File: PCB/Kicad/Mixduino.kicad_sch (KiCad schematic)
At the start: 4 parts

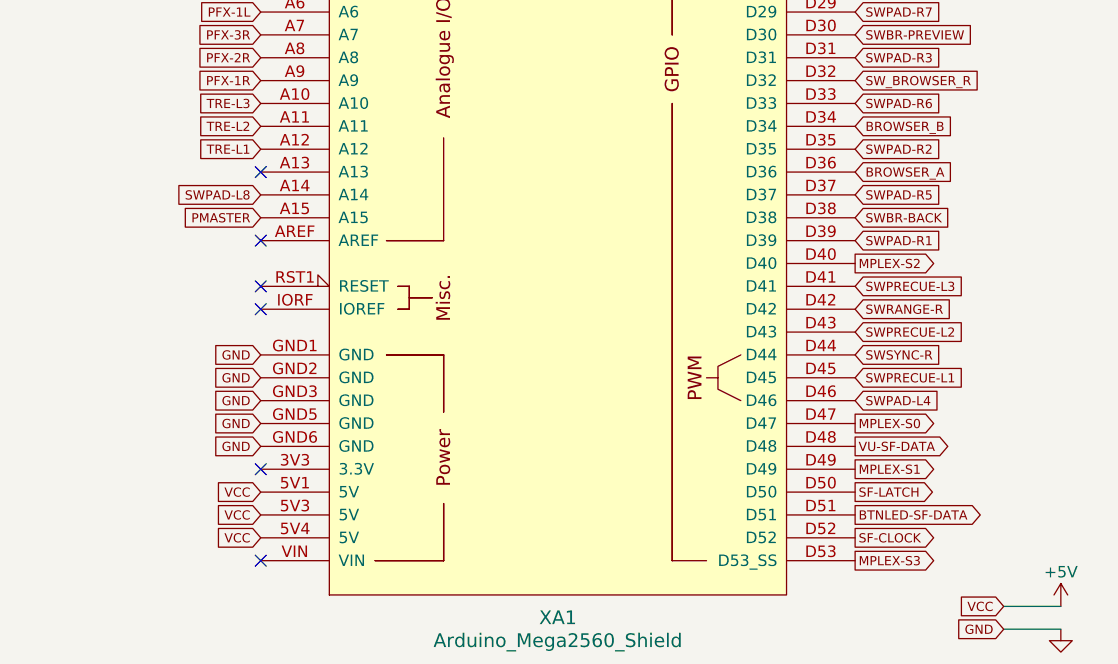
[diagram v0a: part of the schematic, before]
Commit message: mistake fixed
added another latch pin for feedback leds SReg.
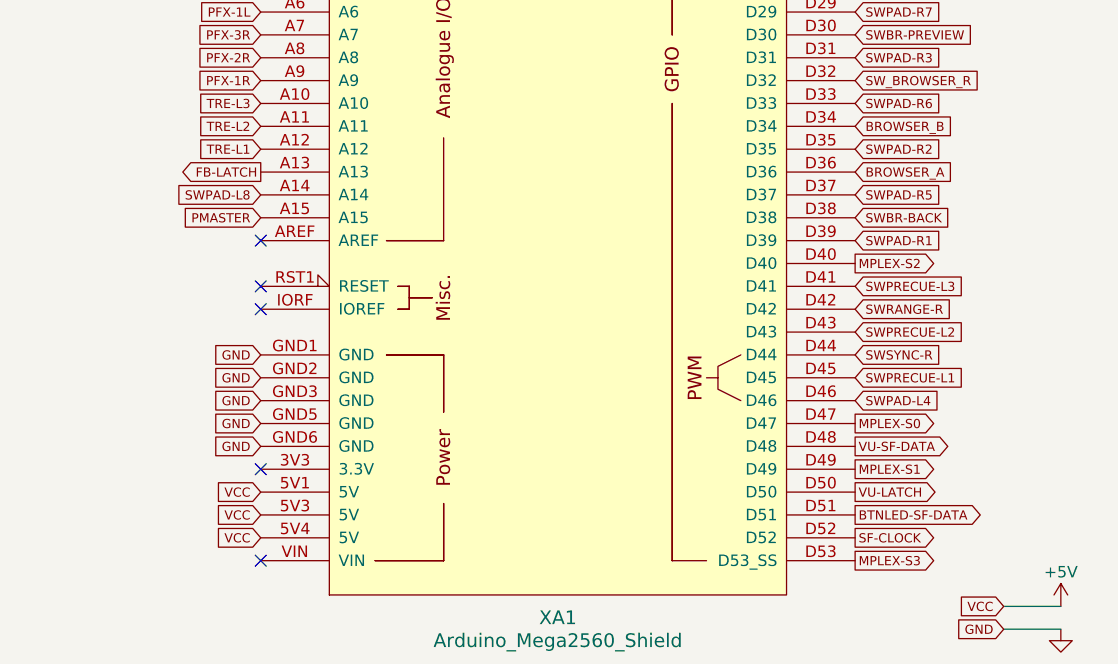
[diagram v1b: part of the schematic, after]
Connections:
- net FB-LATCH: now reaches XA1.A13
- net SF-LATCH renamed VU-LATCH
- no-connect marks 10 -> 9
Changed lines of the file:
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@@
   (no_connect (at 127.635 64.77))
   (no_connect (at 127.635 67.31))
-  (no_connect (at 127.635 105.41))
   (no_connect (at 127.635 113.03))
   (no_connect (at 127.635 118.11))
@@
     )
   )
+  (global_label "FB-LATCH" (shape output) (at 127.635 105.41 180)
+    (effects (font (size 1.016 1.016)) (justify right))
+    (property "Intersheet References" "${INTERSHEET_REFS}" (id 0) (at 119.9473 105.4735 0)
+      (effects (font (size 1.016 1.016)) (justify right) hide)
+    )
+  )
   (global_label "SWPAD-L8" (shape input) (at 127.635 107.95 180)
     (effects (font (size 1.016 1.016)) (justify right))
@@
     )
   )
-  (global_label "SF-LATCH" (shape output) (at 193.675 140.97 0)
+  (global_label "VU-LATCH" (shape output) (at 193.675 140.97 0)
     (effects (font (size 1.016 1.016)) (justify left))
     (property "Intersheet References" "${INTERSHEET_REFS}" (id 0) (at 203.2496 140.9065 0)

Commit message: schematic updated
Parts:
- removed IC-POTS-1: 74HC4067D,653, Library:SOIC-24W_7.5x15.4mm_P1.27mm, symbol mixduino-mk2:74HC4067D,653
- added IC-MPLEX-1: MP-POTS, Library:SOIC-24W_7.5x15.4mm_P1.27mm, symbol mixduino-mk2:74HC4067D,653
- added IC-MPLEX-2: MP-BTNS, Library:SOIC-24W_7.5x15.4mm_P1.27mm, symbol mixduino-mk2:74HC4067D,653
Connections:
- net +5V: now also IC-MPLEX-1.24 (VCC), IC-MPLEX-2.24 (VCC)
- net BAS-L1: now also IC-MPLEX-1.21 (Y10)
- net BAS-L2: now also IC-MPLEX-1.20 (Y11)
- net BAS-L3: now also IC-MPLEX-1.19 (Y12)
- net FADER-L1: now also IC-MPLEX-1.8 (Y1)
- net FADER-L2: now also IC-MPLEX-1.7 (Y2)
- net FADER-L3: now also IC-MPLEX-1.6 (Y3)
- net FB-LATCH: now also XA1.D5; no longer XA1.A13
- net FILTER-L1: now also IC-MPLEX-1.2 (Y7)
- net FILTER-L2: now also IC-MPLEX-1.23 (Y8)
- net FILTER-L3: now also IC-MPLEX-1.22 (Y9)
- net GAIN-L1: now also XA1.A10; no longer XA1.A3
- net GAIN-L2: now also XA1.A9; no longer XA1.A2
- net GAIN-L3: now also XA1.A8; no longer XA1.A1
- net GND: now also IC-MPLEX-1.12 (GND), IC-MPLEX-1.15 (~E), IC-MPLEX-2.12 (GND), IC-MPLEX-2.15 (~E)
- net MID-L1: now also IC-MPLEX-1.18 (Y13)
- net MID-L2: now also IC-MPLEX-1.17 (Y14)
- net MID-L3: now also IC-MPLEX-1.16 (Y15)
- net MPLEX-A0: now also IC-MPLEX-1.1 (Z)
- net MPLEX-S0: now also IC-MPLEX-1.10 (S0), IC-MPLEX-2.10 (S0)
- net MPLEX-S1: now also IC-MPLEX-1.11 (S1), IC-MPLEX-2.11 (S1)
- net MPLEX-S2: now also IC-MPLEX-1.14 (S2), IC-MPLEX-2.14 (S2)
- net MPLEX-S3: now also IC-MPLEX-1.13 (S3), IC-MPLEX-2.13 (S3)
- net PFX-1L: now also XA1.A4; no longer XA1.A6
- net PFX-1R: now also XA1.A7; no longer XA1.A9
- net PFX-2L: now also XA1.A3; no longer XA1.A5
- net PFX-2R: now also XA1.A6; no longer XA1.A8
- net PFX-3L: now also XA1.A2; no longer XA1.A4
- net PFX-3R: now also XA1.A5; no longer XA1.A7
- net PITCH-L: now also IC-MPLEX-1.9 (Y0)
- net PITCH-R: now also IC-MPLEX-1.3 (Y6)
- net PMASTER: now also XA1.A14; no longer XA1.A15
- net PMIX-HP: now also IC-MPLEX-1.5 (Y4)
- net PVOL-HP: now also IC-MPLEX-1.4 (Y5)
- net SWCUE-L: now also IC-MPLEX-2.19 (Y12); no longer XA1.D22
- net SWCUE-R: now also XA1.D28; no longer XA1.D15 (D15_RX3)
- net SWFX1-L: now also XA1.D8; no longer XA1.D7
- net SWFX2-L: now also XA1.D7; no longer XA1.D6
- net SWFX3-L: now also XA1.D6; no longer XA1.D5
- net SWPAD-L1: now also IC-MPLEX-2.2 (Y7); no longer XA1.D24
- net SWPAD-L2: now also IC-MPLEX-2.3 (Y6); no longer XA1.D19 (D19_RX1)
- net SWPAD-L3: now also IC-MPLEX-2.4 (Y5); no longer XA1.D26
- net SWPAD-L4: now also IC-MPLEX-2.5 (Y4); no longer XA1.D46
- net SWPAD-L5: now also IC-MPLEX-2.6 (Y3); no longer XA1.D14 (D14_TX3)
- net SWPAD-L6: now also IC-MPLEX-2.7 (Y2); no longer XA1.D28
- net SWPAD-L7: now also IC-MPLEX-2.8 (Y1); no longer XA1.D3 (D3_INT1)
- net SWPAD-L8: now also IC-MPLEX-2.9 (Y0); no longer XA1.A14
- net SWPLAY-L: now also IC-MPLEX-2.20 (Y11); no longer XA1.D18 (D18_TX1)
- net SWPRECUE-L1: now also IC-MPLEX-2.16 (Y15); no longer XA1.D45
- net SWPRECUE-L2: now also IC-MPLEX-2.17 (Y14); no longer XA1.D43
- net SWPRECUE-L3: now also IC-MPLEX-2.18 (Y13); no longer XA1.D41
- net SWRANGE-L: now also IC-MPLEX-2.21 (Y10); no longer XA1.D16 (D16_TX2)
- net SWSHIFT: now also IC-MPLEX-2.22 (Y9); no longer XA1.D17 (D17_RX2)
- net SWSYNC-L: now also IC-MPLEX-2.23 (Y8); no longer XA1.D8
- net TRE-L1: now also XA1.A11; no longer XA1.A12
- net TRE-L2: now also XA1.A12; no longer XA1.A11
- net TRE-L3: now also XA1.A13; no longer XA1.A10
- net BROWSER_A renamed R_BROWSER_A
- net BROWSER_B renamed R_BROWSER_B
- net NP_SIG_LEFT renamed NP_L_PADS_DATA
- net NP_SIG_RIGTH renamed NP_R_PADS_DATA
- new net L_BROWSER_A: XA1.D43
- new net L_BROWSER_B: XA1.D41
- new net MPLEX-A1: IC-MPLEX-2.1 (Z), XA1.A1
- new net NP_L_FB_DATA: XA1.D3 (D3_INT1)
- new net NP_R_FB_DATA: XA1.D24
- new net SWLOOP-L: XA1.D22
- new net SWLOOP-R: XA1.D26
- no-connect marks 9 -> 18
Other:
- moved on the sheet: TB1, TB2, XA1

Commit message: schematic updated
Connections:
- net BAS-L1: now also IC-MPLEX-1.4 (Y5); no longer IC-MPLEX-1.21 (Y10)
- net BAS-L2: now also IC-MPLEX-1.2 (Y7); no longer IC-MPLEX-1.20 (Y11)
- net BAS-L3: now also IC-MPLEX-1.21 (Y10); no longer IC-MPLEX-1.19 (Y12)
- net FADER-L2: now also IC-MPLEX-1.9 (Y0); no longer IC-MPLEX-1.7 (Y2)
- net FADER-L3: now also IC-MPLEX-1.16 (Y15); no longer IC-MPLEX-1.6 (Y3)
- net FB-LATCH: now also XA1.D43; no longer XA1.D5
- net FILTER-L1: now also IC-MPLEX-1.6 (Y3); no longer IC-MPLEX-1.2 (Y7)
- net FILTER-L2: now also IC-MPLEX-1.5 (Y4); no longer IC-MPLEX-1.23 (Y8)
- net FILTER-L3: now also IC-MPLEX-1.20 (Y11); no longer IC-MPLEX-1.22 (Y9)
- net GAIN-L1: now also XA1.A5; no longer XA1.A10
- net GAIN-L2: now also XA1.A4; no longer XA1.A9
- net GAIN-L3: now also XA1.A3; no longer XA1.A8
- net L_BROWSER_A: now also XA1.D4; no longer XA1.D43
- net L_BROWSER_B: now also XA1.D5; no longer XA1.D41
- net MID-L1: now also IC-MPLEX-1.3 (Y6); no longer IC-MPLEX-1.18 (Y13)
- net MID-L2: now also IC-MPLEX-1.23 (Y8); no longer IC-MPLEX-1.17 (Y14)
- net MID-L3: now also IC-MPLEX-1.22 (Y9); no longer IC-MPLEX-1.16 (Y15)
- net PFX-1L: now also XA1.A8; no longer XA1.A4
- net PFX-1R: now also XA1.A2; no longer XA1.A7
- net PFX-2L: now also XA1.A9; no longer XA1.A3
- net PFX-2R: now also XA1.A7; no longer XA1.A6
- net PFX-3L: now also XA1.A10; no longer XA1.A2
- net PFX-3R: now also XA1.A6; no longer XA1.A5
- net PITCH-L: now also IC-MPLEX-1.7 (Y2); no longer IC-MPLEX-1.9 (Y0)
- net PITCH-R: now also IC-MPLEX-1.19 (Y12); no longer IC-MPLEX-1.3 (Y6)
- net PMIX-HP: now also IC-MPLEX-1.17 (Y14); no longer IC-MPLEX-1.5 (Y4)
- net PVOL-HP: now also IC-MPLEX-1.18 (Y13); no longer IC-MPLEX-1.4 (Y5)
- net SW-DECK-SEL: now also XA1.D41; no longer XA1.D4
- net SWCUE-L: now also IC-MPLEX-2.2 (Y7); no longer IC-MPLEX-2.19 (Y12)
- net SWLOOP-L: now also IC-MPLEX-2.6 (Y3); no longer XA1.D22
- net SWPAD-L1: now also IC-MPLEX-2.22 (Y9); no longer IC-MPLEX-2.2 (Y7)
- net SWPAD-L2: now also IC-MPLEX-2.20 (Y11); no longer IC-MPLEX-2.3 (Y6)
- net SWPAD-L3: now also IC-MPLEX-2.18 (Y13); no longer IC-MPLEX-2.4 (Y5)
- net SWPAD-L4: now also IC-MPLEX-2.17 (Y14); no longer IC-MPLEX-2.5 (Y4)
- net SWPAD-L5: now also IC-MPLEX-2.23 (Y8); no longer IC-MPLEX-2.6 (Y3)
- net SWPAD-L6: now also IC-MPLEX-2.21 (Y10); no longer IC-MPLEX-2.7 (Y2)
- net SWPAD-L7: now also IC-MPLEX-2.19 (Y12); no longer IC-MPLEX-2.8 (Y1)
- net SWPAD-L8: now also IC-MPLEX-2.16 (Y15); no longer IC-MPLEX-2.9 (Y0)
- net SWPAD-R4: now also XA1.D25; no longer XA1.D27
- net SWPAD-R8: now also XA1.D27; no longer XA1.D25
- net SWPLAY-L: now also IC-MPLEX-2.3 (Y6); no longer IC-MPLEX-2.20 (Y11)
- net SWPRECUE-L1: now also IC-MPLEX-2.8 (Y1); no longer IC-MPLEX-2.16 (Y15)
- net SWPRECUE-L2: now also IC-MPLEX-2.9 (Y0); no longer IC-MPLEX-2.17 (Y14)
- net SWPRECUE-L3: now also XA1.D45; no longer IC-MPLEX-2.18 (Y13)
- net SWRANGE-L: now also IC-MPLEX-2.4 (Y5); no longer IC-MPLEX-2.21 (Y10)
- net SWSHIFT: now also IC-MPLEX-2.7 (Y2); no longer IC-MPLEX-2.22 (Y9)
- net SWSYNC-L: now also IC-MPLEX-2.5 (Y4); no longer IC-MPLEX-2.23 (Y8)

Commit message: tracking WIP
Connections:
- net L_BROWSER_A: now also XA1.D13; no longer XA1.D4
- net L_BROWSER_B: now also XA1.D12; no longer XA1.D5
- net MPLEX-A0: now also XA1.A2; no longer XA1.A0
- net PFX-1R: now also XA1.A0; no longer XA1.A2
- net PFX-2L: now also XA1.A7; no longer XA1.A9
- net PFX-2R: now also XA1.A9; no longer XA1.A7
- net PFX-3L: now also XA1.A6; no longer XA1.A10
- net PFX-3R: now also XA1.A10; no longer XA1.A6
- net SWFX1-L: now also XA1.D7; no longer XA1.D8
- net SWFX2-L: now also XA1.D8; no longer XA1.D7
- net SWFX2-R: now also XA1.D4; no longer XA1.D12
- net SWFX3-L: now also XA1.D9; no longer XA1.D6
- net SWFX3-R: now also XA1.D5; no longer XA1.D13
- net SWPLAY-R: now also XA1.D22; no longer XA1.D9
- net TRE-L1: now also XA1.A13; no longer XA1.A11
- net TRE-L3: now also XA1.A11; no longer XA1.A13
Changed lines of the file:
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@@
   (no_connect (at 127.635 127.635))
   (no_connect (at 127.635 137.795))
-  (no_connect (at 193.675 59.055))
+  (no_connect (at 193.675 38.735))
   (no_connect (at 193.675 120.015))
   (wire (pts (xy 62.23 178.435) (xy 68.58 178.435))
@@
     )
   )
-  (global_label "MPLEX-A0" (shape input) (at 127.635 61.595 180)
-    (effects (font (size 1.016 1.016)) (justify right))
-    (property "Intersheet References" "${INTERSHEET_REFS}" (id 0) (at 117.7217 61.5315 0)
-      (effects (font (size 1.016 1.016)) (justify right) hide)
+  (global_label "PFX-1R" (shape input) (at 127.635 61.595 180)
+    (effects (font (size 1.016 1.016)) (justify right))
+    (property "Intersheet References" "${INTERSHEET_REFS}" (id 0) (at 337.185 5.715 0)
+      (effects (font (size 1.27 1.27)) (justify left) hide)
     )
   )
   (global_label "MPLEX-A1" (shape input) (at 127.635 64.135 180)
     (effects (font (size 1.016 1.016)) (justify right))
-    (property "Intersheet References" "${INTERSHEET_REFS}" (id 0) (at 119.2216 64.1985 0)
-      (effects (font (size 1.016 1.016)) (justify right) hide)
-    )
-  )
-  (global_label "PFX-1R" (shape input) (at 127.635 66.675 180)
-    (effects (font (size 1.016 1.016)) (justify right))
-    (property "Intersheet References" "${INTERSHEET_REFS}" (id 0) (at 337.185 122.555 0)
-      (effects (font (size 1.27 1.27)) (justify left) hide)
+    (property "Intersheet References" "${INTERSHEET_REFS}" (id 0) (at 119.2216 64.0715 0)
+      (effects (font (size 1.016 1.016)) (justify right) hide)
+    )
+  )
+  (global_label "MPLEX-A0" (shape input) (at 127.635 66.675 180)
+    (effects (font (size 1.016 1.016)) (justify right))
+    (property "Intersheet References" "${INTERSHEET_REFS}" (id 0) (at 117.7217 66.7385 0)
+      (effects (font (size 1.016 1.016)) (justify right) hide)
     )
   )
@@
     )
   )
-  (global_label "PFX-3R" (shape input) (at 127.635 76.835 180)
-    (effects (font (size 1.016 1.016)) (justify right))
-    (property "Intersheet References" "${INTERSHEET_REFS}" (id 0) (at 337.185 142.875 0)
-      (effects (font (size 1.27 1.27)) (justify left) hide)
-    )
-  )
-  (global_label "PFX-2R" (shape input) (at 127.635 79.375 180)
-    (effects (font (size 1.016 1.016)) (justify right))
-    (property "Intersheet References" "${INTERSHEET_REFS}" (id 0) (at 337.185 140.335 0)
-      (effects (font (size 1.27 1.27)) (justify left) hide)
+  (global_label "PFX-3L" (shape input) (at 127.635 76.835 180)
+    (effects (font (size 1.016 1.016)) (justify right))
+    (property "Intersheet References" "${INTERSHEET_REFS}" (id 0) (at 119.8021 76.7715 0)
+      (effects (font (size 1.016 1.016)) (justify right) hide)
+    )
+  )
+  (global_label "PFX-2L" (shape input) (at 127.635 79.375 180)
+    (effects (font (size 1.016 1.016)) (justify right))
+    (property "Intersheet References" "${INTERSHEET_REFS}" (id 0) (at 119.8021 79.3115 0)
+      (effects (font (size 1.016 1.016)) (justify right) hide)
     )
   )
@@
     )
   )
-  (global_label "PFX-2L" (shape input) (at 127.635 84.455 180)
-    (effects (font (size 1.016 1.016)) (justify right))
-    (property "Intersheet References" "${INTERSHEET_REFS}" (id 0) (at 119.8021 84.5185 0)
-      (effects (font (size 1.016 1.016)) (justify right) hide)
-    )
-  )
-  (global_label "PFX-3L" (shape input) (at 127.635 86.995 180)
-    (effects (font (size 1.016 1.016)) (justify right))
-    (property "Intersheet References" "${INTERSHEET_REFS}" (id 0) (at 119.8021 87.0585 0)
-      (effects (font (size 1.016 1.016)) (justify right) hide)
-    )
-  )
-  (global_label "TRE-L1" (shape input) (at 127.635 89.535 180)
-    (effects (font (size 1.016 1.016)) (justify right))
-    (property "Intersheet References" "${INTERSHEET_REFS}" (id 0) (at 119.9473 89.4715 0)
+  (global_label "PFX-2R" (shape input) (at 127.635 84.455 180)
+    (effects (font (size 1.016 1.016)) (justify right))
+    (property "Intersheet References" "${INTERSHEET_REFS}" (id 0) (at 337.185 23.495 0)
+      (effects (font (size 1.27 1.27)) (justify left) hide)
+    )
+  )
+  (global_label "PFX-3R" (shape input) (at 127.635 86.995 180)
+    (effects (font (size 1.016 1.016)) (justify right))
+    (property "Intersheet References" "${INTERSHEET_REFS}" (id 0) (at 337.185 20.955 0)
+      (effects (font (size 1.27 1.27)) (justify left) hide)
+    )
+  )
+  (global_label "TRE-L3" (shape input) (at 127.635 89.535 180)
+    (effects (font (size 1.016 1.016)) (justify right))
+    (property "Intersheet References" "${INTERSHEET_REFS}" (id 0) (at 119.9473 89.5985 0)
       (effects (font (size 1.016 1.016)) (justify right) hide)
     )
@@
   (global_label "TRE-L2" (shape input) (at 127.635 92.075 180)
     (effects (font (size 1.016 1.016)) (justify right))
-    (property "Intersheet References" "${INTERSHEET_REFS}" (id 0) (at 119.9473 92.0115 0)
-      (effects (font (size 1.016 1.016)) (justify right) hide)
-    )
-  )
-  (global_label "TRE-L3" (shape input) (at 127.635 94.615 180)
-    (effects (font (size 1.016 1.016)) (justify right))
-    (property "Intersheet References" "${INTERSHEET_REFS}" (id 0) (at 119.9473 94.5515 0)
+    (property "Intersheet References" "${INTERSHEET_REFS}" (id 0) (at 119.9473 92.1385 0)
+      (effects (font (size 1.016 1.016)) (justify right) hide)
+    )
+  )
+  (global_label "TRE-L1" (shape input) (at 127.635 94.615 180)
+    (effects (font (size 1.016 1.016)) (justify right))
+    (property "Intersheet References" "${INTERSHEET_REFS}" (id 0) (at 119.9473 94.6785 0)
       (effects (font (size 1.016 1.016)) (justify right) hide)
     )
@@
     )
   )
-  (global_label "L_BROWSER_A" (shape input) (at 193.675 33.655 0)
-    (effects (font (size 1.016 1.016)) (justify left))
-    (property "Intersheet References" "${INTERSHEET_REFS}" (id 0) (at 204.4107 33.7185 0)
-      (effects (font (size 1.016 1.016)) (justify left) hide)
-    )
-  )
-  (global_label "L_BROWSER_B" (shape input) (at 193.675 36.195 0)
-    (effects (font (size 1.016 1.016)) (justify left))
-    (property "Intersheet References" "${INTERSHEET_REFS}" (id 0) (at 204.5559 36.2585 0)
-      (effects (font (size 1.016 1.016)) (justify left) hide)
-    )
-  )
-  (global_label "SWFX3-L" (shape input) (at 193.675 38.735 0)
-    (effects (font (size 1.016 1.016)) (justify left))
-    (property "Intersheet References" "${INTERSHEET_REFS}" (id 0) (at 81.915 186.055 0)
-      (effects (font (size 1.27 1.27)) hide)
-    )
-  )
-  (global_label "SWFX2-L" (shape input) (at 193.675 41.275 0)
-    (effects (font (size 1.016 1.016)) (justify left))
-    (property "Intersheet References" "${INTERSHEET_REFS}" (id 0) (at 81.915 172.085 0)
-      (effects (font (size 1.27 1.27)) hide)
-    )
-  )
-  (global_label "SWFX1-L" (shape input) (at 193.675 43.815 0)
-    (effects (font (size 1.016 1.016)) (justify left))
-    (property "Intersheet References" "${INTERSHEET_REFS}" (id 0) (at 81.915 158.115 0)
-      (effects (font (size 1.27 1.27)) hide)
-    )
-  )
-  (global_label "SWPLAY-R" (shape input) (at 193.675 46.355 0)
-    (effects (font (size 1.016 1.016)) (justify left))
-    (property "Intersheet References" "${INTERSHEET_REFS}" (id 0) (at 47.625 13.335 0)
+  (global_label "SWFX2-R" (shape input) (at 193.675 33.655 0)
+    (effects (font (size 1.016 1.016)) (justify left))
+    (property "Intersheet References" "${INTERSHEET_REFS}" (id 0) (at 47.625 -97.155 0)
+      (effects (font (size 1.27 1.27)) (justify right) hide)
+    )
+  )
+  (global_label "SWFX3-R" (shape input) (at 193.675 36.195 0)
+    (effects (font (size 1.016 1.016)) (justify left))
+    (property "Intersheet References" "${INTERSHEET_REFS}" (id 0) (at 47.625 -111.125 0)
+      (effects (font (size 1.27 1.27)) (justify right) hide)
+    )
+  )
+  (global_label "SWFX1-L" (shape input) (at 193.675 41.275 0)
+    (effects (font (size 1.016 1.016)) (justify left))
+    (property "Intersheet References" "${INTERSHEET_REFS}" (id 0) (at 81.915 -73.025 0)
+      (effects (font (size 1.27 1.27)) hide)
+    )
+  )
+  (global_label "SWFX2-L" (shape input) (at 193.675 43.815 0)
+    (effects (font (size 1.016 1.016)) (justify left))
+    (property "Intersheet References" "${INTERSHEET_REFS}" (id 0) (at 81.915 -86.995 0)
+      (effects (font (size 1.27 1.27)) hide)
+    )
+  )
+  (global_label "SWFX3-L" (shape input) (at 193.675 46.355 0)
+    (effects (font (size 1.016 1.016)) (justify left))
+    (property "Intersheet References" "${INTERSHEET_REFS}" (id 0) (at 81.915 -100.965 0)
       (effects (font (size 1.27 1.27)) hide)
     )
@@
     )
   )
-  (global_label "SWFX2-R" (shape input) (at 193.675 53.975 0)
-    (effects (font (size 1.016 1.016)) (justify left))
-    (property "Intersheet References" "${INTERSHEET_REFS}" (id 0) (at 47.625 -76.835 0)
-      (effects (font (size 1.27 1.27)) (justify right) hide)
-    )
-  )
-  (global_label "SWFX3-R" (shape input) (at 193.675 56.515 0)
-    (effects (font (size 1.016 1.016)) (justify left))
-    (property "Intersheet References" "${INTERSHEET_REFS}" (id 0) (at 47.625 -90.805 0)
-      (effects (font (size 1.27 1.27)) (justify right) hide)
-    )
-  )
+  (global_label "L_BROWSER_B" (shape input) (at 193.675 53.975 0)
+    (effects (font (size 1.016 1.016)) (justify left))
+    (property "Intersheet References" "${INTERSHEET_REFS}" (id 0) (at 204.5559 53.9115 0)
+      (effects (font (size 1.016 1.016)) (justify left) hide)
+    )
+  )
+  (global_label "L_BROWSER_A" (shape input) (at 193.675 56.515 0)
+    (effects (font (size 1.016 1.016)) (justify left))
+    (property "Intersheet References" "${INTERSHEET_REFS}" (id 0) (at 204.4107 56.4515 0)
+      (effects (font (size 1.016 1.016)) (justify left) hide)
+    )
+  )
+  (global_label "SWPLAY-R" (shape input) (at 193.675 59.055 0)
+    (effects (font (size 1.016 1.016)) (justify left))
+    (property "Intersheet References" "${INTERSHEET_REFS}" (id 0) (at 47.625 26.035 0)
+      (effects (font (size 1.27 1.27)) hide)
+    )
+  )
